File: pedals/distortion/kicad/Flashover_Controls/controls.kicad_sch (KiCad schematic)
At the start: 20 parts, among them SW1 PEC11R-4215F-S0024, SW2 PEC11R-4215F-S0024, SW3 PEC11R-4215F-S0024, SW4 Soft/Hard

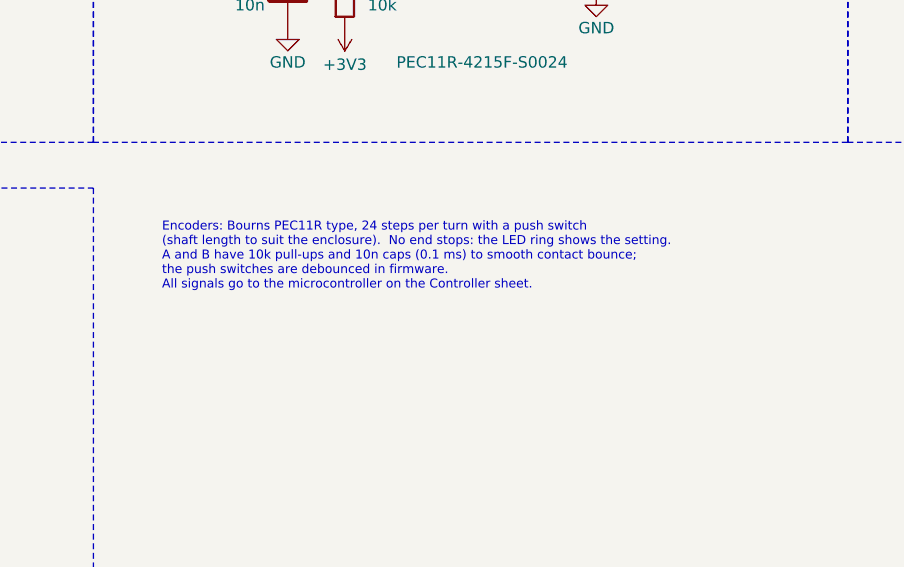
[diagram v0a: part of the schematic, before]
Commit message: Split Flashover into main and control boards; place parts
Main board (Flashover): audio, controller, pots, MIDI, bypass and the five
top-mounted jacks.  Control board (Flashover_Controls): encoders, LED rings,
LED driver, Soft/Hard button and panel LEDs.  J7/J8 2x10 board connector,
M3 mounting holes, regulator laid flat.  Placement only, not yet routed.

Co-Authored-By: Claude Opus 5.5 <noreply@anthropic.com>
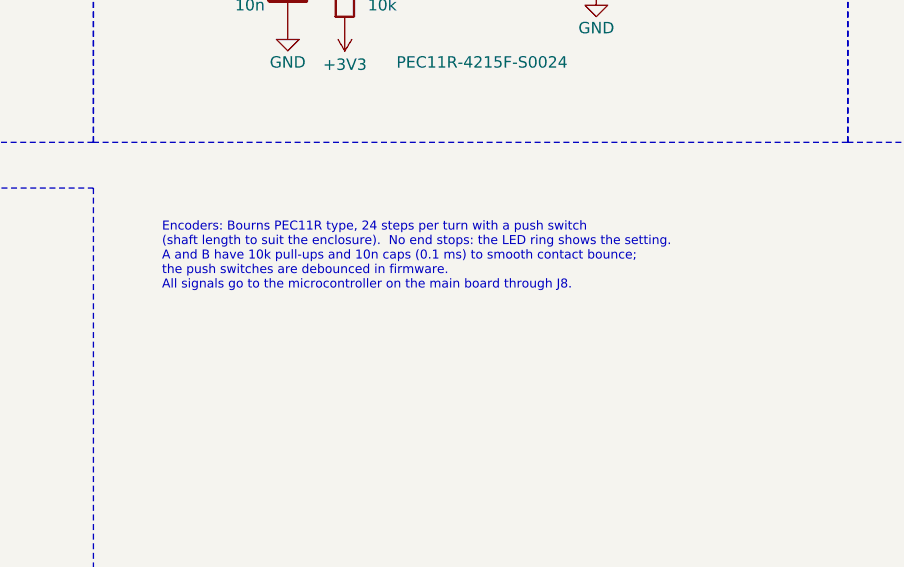
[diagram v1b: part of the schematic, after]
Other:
- note added: "Encoders: Bourns PEC11R type, 24 steps per turn with a push switch (shaft length to suit the enclosure). No end stops: the LED ring shows the setting. A and B have 10k pull-ups and 10n caps (0.1 ms) to smooth contact bounce; the push switches are debounced in firmware. All signals go to the microcontroller on the main board through J8."
- note removed: "Encoders: Bourns PEC11R type, 24 steps per turn with a push switch (shaft length to suit the enclosure). No end stops: the LED ring shows the setting. A and B have 10k pull-ups and 10n caps (0.1 ms) to smooth contact bounce; the push switches are debounced in firmware. All signals go to the microcontroller on the Controller sheet."

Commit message: Fit Flashover to the 1590BB and part datasheets
- Correct PEC11R encoder footprint (legs 13.2 mm apart) in a new
  GreywireStudio footprint library; swap it onto the control board and
  bend three tracks around the wider legs
- Move MIDI jacks to the side walls, spread the top jacks out and put
  their fronts against the wall; re-autoroute the main board
- gen_pcb.py rebuilds the control board only with --controls
- Add fit check, board heights and drilling guide to the status note;
  update the product document

Co-Authored-By: Claude Opus 5.5 <noreply@anthropic.com>
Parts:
- SW1, SW2, SW3: value PEC11R-4215F-S0024 -> PEC11R-4220F-S0024; footprint Rotary_Encoder:RotaryEncoder_Alps_EC11E-Switch_Vertical_H20mm -> GreywireStudio:RotaryEncoder_Bourns_PEC11R-4xxxF-Sxxxx_Vertical
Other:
- note added: "Encoders: Bourns PEC11R type, 24 steps per turn with a push switch (20 mm shaft: body against the inside of the panel, nut outside). No end stops: the LED ring shows the setting. A and B have 10k pull-ups and 10n caps (0.1 ms) to smooth contact bounce; the push switches are debounced in firmware. All signals go to the microcontroller on the main board through J8."
- note removed: "Encoders: Bourns PEC11R type, 24 steps per turn with a push switch (shaft length to suit the enclosure). No end stops: the LED ring shows the setting. A and B have 10k pull-ups and 10n caps (0.1 ms) to smooth contact bounce; the push switches are debounced in firmware. All signals go to the microcontroller on the main board through J8."
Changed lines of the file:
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@@
 		(effects (font (size 1 1)) (justify left))
 	)
-	(text "Encoders: Bourns PEC11R type, 24 steps per turn with a push switch\n(shaft length to suit the enclosure).  No end stops: the LED ring shows the setting.\nA and B have 10k pull-ups and 10n caps (0.1 ms) to smooth contact bounce;\nthe push switches are debounced in firmware.\nAll signals go to the microcontroller on the main board through J8."
+	(text "Encoders: Bourns PEC11R type, 24 steps per turn with a push switch\n(20 mm shaft: body against the inside of the panel, nut outside).  No end stops: the LED ring shows the setting.\nA and B have 10k pull-ups and 10n caps (0.1 ms) to smooth contact bounce;\nthe push switches are debounced in firmware.\nAll signals go to the microcontroller on the main board through J8."
 		(exclude_from_sim no)
 		(at 111.76 119.38 0)
@@
 			(effects (font (size 1.27 1.27)))
 		)
-		(property "Value" "PEC11R-4215F-S0024"
+		(property "Value" "PEC11R-4220F-S0024"
 			(at 63.5 97.79 0)
 			(show_name no)
@@
 			(effects (font (size 1.27 1.27)))
 		)
-		(property "Footprint" "Rotary_Encoder:RotaryEncoder_Alps_EC11E-Switch_Vertical_H20mm"
+		(property "Footprint" "GreywireStudio:RotaryEncoder_Bourns_PEC11R-4xxxF-Sxxxx_Vertical"
 			(at 66.04 83.82 0)
 			(hide yes)
@@
 			(effects (font (size 1.27 1.27)))
 		)
-		(property "Value" "PEC11R-4215F-S0024"
+		(property "Value" "PEC11R-4220F-S0024"
 			(at 147.32 97.79 0)
 			(show_name no)
@@
 			(effects (font (size 1.27 1.27)))
 		)
-		(property "Footprint" "Rotary_Encoder:RotaryEncoder_Alps_EC11E-Switch_Vertical_H20mm"
+		(property "Footprint" "GreywireStudio:RotaryEncoder_Bourns_PEC11R-4xxxF-Sxxxx_Vertical"
 			(at 149.86 83.82 0)
 			(hide yes)
@@
 			(effects (font (size 1.27 1.27)))
 		)
-		(property "Value" "PEC11R-4215F-S0024"
+		(property "Value" "PEC11R-4220F-S0024"
 			(at 231.14 97.79 0)
 			(show_name no)
@@
 			(effects (font (size 1.27 1.27)))
 		)
-		(property "Footprint" "Rotary_Encoder:RotaryEncoder_Alps_EC11E-Switch_Vertical_H20mm"
+		(property "Footprint" "GreywireStudio:RotaryEncoder_Bourns_PEC11R-4xxxF-Sxxxx_Vertical"
 			(at 233.68 83.82 0)
 			(hide yes)
